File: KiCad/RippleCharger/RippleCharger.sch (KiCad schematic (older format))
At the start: 0 parts

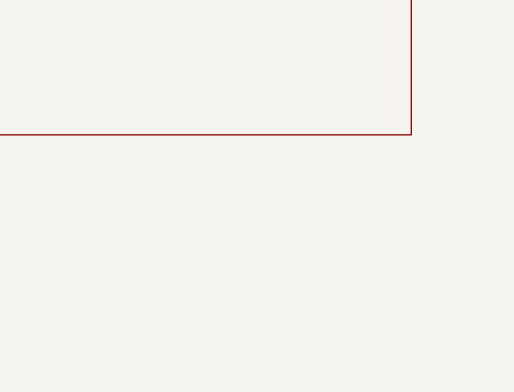
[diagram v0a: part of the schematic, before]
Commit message: Update PCB layout m include relay footprint, board outlook.Modify Main 0049 code and add CV function
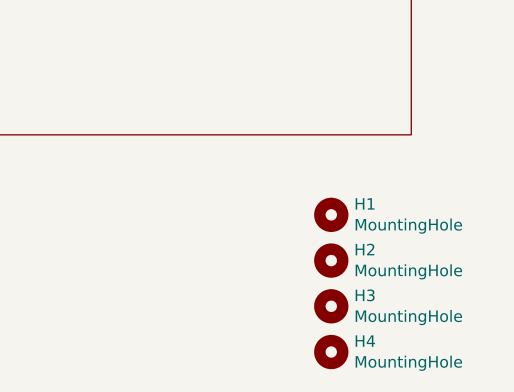
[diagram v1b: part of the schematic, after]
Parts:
- added H1, H2, H3, H4: MountingHole, MountingHole:MountingHole_3.2mm_M3_DIN965_Pad_TopBottom, symbol Mechanical:MountingHole
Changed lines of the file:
@@
 F1 "Battery.sch" 50
 $EndSheet
+$Comp
+L Mechanical:MountingHole H?
+U 1 1 61790F4D
+P 6300 4650
+AR Path="/613448A2/61790F4D" Ref="H?"  Part="1"
+AR Path="/61790F4D" Ref="H1"  Part="1"
+F 0 "H1" H 6400 4696 50  0000 L CNN
+F 1 "MountingHole" H 6400 4605 50  0000 L CNN
+F 2 "MountingHole:MountingHole_3.2mm_M3_DIN965_Pad_TopBottom" H 6300 4650 50  0001 C CNN
+F 3 "~" H 6300 4650 50  0001 C CNN
+	1    6300 4650
+	1    0    0    -1
+$EndComp
+$Comp
+L Mechanical:MountingHole H?
+U 1 1 61790F53
+P 6300 4850
+AR Path="/613448A2/61790F53" Ref="H?"  Part="1"
+AR Path="/61790F53" Ref="H2"  Part="1"
+F 0 "H2" H 6400 4896 50  0000 L CNN
+F 1 "MountingHole" H 6400 4805 50  0000 L CNN
+F 2 "MountingHole:MountingHole_3.2mm_M3_DIN965_Pad_TopBottom" H 6300 4850 50  0001 C CNN
+F 3 "~" H 6300 4850 50  0001 C CNN
+	1    6300 4850
+	1    0    0    -1
+$EndComp
+$Comp
+L Mechanical:MountingHole H?
+U 1 1 61790F59
+P 6300 5050
+AR Path="/613448A2/61790F59" Ref="H?"  Part="1"
+AR Path="/61790F59" Ref="H3"  Part="1"
+F 0 "H3" H 6400 5096 50  0000 L CNN
+F 1 "MountingHole" H 6400 5005 50  0000 L CNN
+F 2 "MountingHole:MountingHole_3.2mm_M3_DIN965_Pad_TopBottom" H 6300 5050 50  0001 C CNN
+F 3 "~" H 6300 5050 50  0001 C CNN
+	1    6300 5050
+	1    0    0    -1
+$EndComp
+$Comp
+L Mechanical:MountingHole H?
+U 1 1 61790F5F
+P 6300 5250
+AR Path="/613448A2/61790F5F" Ref="H?"  Part="1"
+AR Path="/61790F5F" Ref="H4"  Part="1"
+F 0 "H4" H 6400 5296 50  0000 L CNN
+F 1 "MountingHole" H 6400 5205 50  0000 L CNN
+F 2 "MountingHole:MountingHole_3.2mm_M3_DIN965_Pad_TopBottom" H 6300 5250 50  0001 C CNN
+F 3 "~" H 6300 5250 50  0001 C CNN
+	1    6300 5250
+	1    0    0    -1
+$EndComp
 $EndSCHEMATC
